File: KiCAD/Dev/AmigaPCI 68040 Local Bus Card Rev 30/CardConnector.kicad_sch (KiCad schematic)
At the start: 29 parts, among them CN100 DIN41612_03x40, CN3 SPI, U10 ICE40HX4K-TQ144, U409F2 W25X20CLSN

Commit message: Start routing PCLB card, Rev 3.0 08-JUL-2024
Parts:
- added C135: 47uF, Capacitor_THT:CP_Radial_D5.0mm_P2.00mm, symbol AmigaPCI-Symbols:CP_Small-Device
- added C137: 0.1uF, Capacitor_SMD:C_0603_1608Metric, symbol Device:C_Small
- added J100: CPU CLOCK, Connector_PinHeader_2.54mm:PinHeader_2x02_P2.54mm_Vertical, symbol Connector_Generic:Conn_02x02_Odd_Even
- added R110, R111: 10k, Resistor_SMD:R_0603_1608Metric, symbol Device:R
- added R112, R113, R114, R115, R116, R117, R118: 22R, Resistor_SMD:R_0603_1608Metric, symbol Device:R
- added X100: 40MHz, Oscillator:Oscillator_SMD_ECS_2520MV-xxx-xx-4Pin_2.5x2.0mm, symbol Oscillator:XO32
- renumbered C16 to C122, C17 to C123, C18 to C124, C19 to C125, C20 to C126, C21 to C127, C22 to C128, C23 to C129, C24 to C130, C25 to C131, C26 to C132, C27 to C133, C28 to C134, C15 to C136, CN3 to CN111, R5 to R106, R6 to R107, R7 to R108, R8 to R109, U10 to U111
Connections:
- net +1V2: now also C135.1
- net +3V3: now also C137.1, R110.1, R111.1, X100.1 (EN), X100.4 (V+)
- net BCLKA: now also R117.2; no longer U111.20 (IO3_13B_GBIN7)
- net GND: now also C135.2, C137.2, J100.1 (Pin_1), J100.3 (Pin_3), X100.2 (GND)
- net PCLKA: now also R118.2; no longer U111.21 (IO3_14A_GBIN6)
- net _RESET: now also U111.47 (IO2_79); no longer U111.49 (IO2_81_GBIN5)
- net CLK40: now reaches U111.128 (IO0_197_GBIN1)
- net CLK40: now also R112.1
- net RAMCLK: now reaches U111.129 (IO0_198_GBIN0)
- net at U111.52 (IO2_82_GBIN4): now also R116.1
- net CLKA: now reaches U111.90 (IO1_138)
- net CLKA: now also J100.2 (Pin_2), R110.2
- net CLKB: now reaches U111.91 (IO1_139)
- net CLKB: now also J100.4 (Pin_4), R111.2
- net at U111.93 (IO1_140_GBIN3): now also R117.1
- net at U111.94 (IO1_141_GBIN2): now also R118.1
- net BCLK renamed BCLKC
- net BCLKC: now also R113.2
- net PCLK renamed PCLKC
- net PCLKC: now also R114.2
- new net: R115.1, U111.49 (IO2_81_GBIN5)
- new net: R114.1, U111.21 (IO3_14A_GBIN6)
- new net: R113.1, U111.20 (IO3_13B_GBIN7)
- new net: R112.2, X100.3 (OUT)
- new net BCLKB: R115.2
- new net PCLKB: R116.2
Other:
- note added: "BYTE SIZING"
- note added: "CLOCK STUFF"
- note added: "J100 CLOCK SPEED SELECTION -------------------------- All Open = 40/80MHz 1-2 = 33/66MHz 3-4 = 25/50MHz 1-2 & 3-4 = 16/32MHz"
- note added: "LOCAL BUS PORT"
- note added: "LOCAL BUS PORT, BYTE SIZING, CLOCKS"
- note removed: "CARD CONNECTOR"
- note removed: "CARD EDGE AND RAM"
- moved on the sheet: CN100, H1, H2

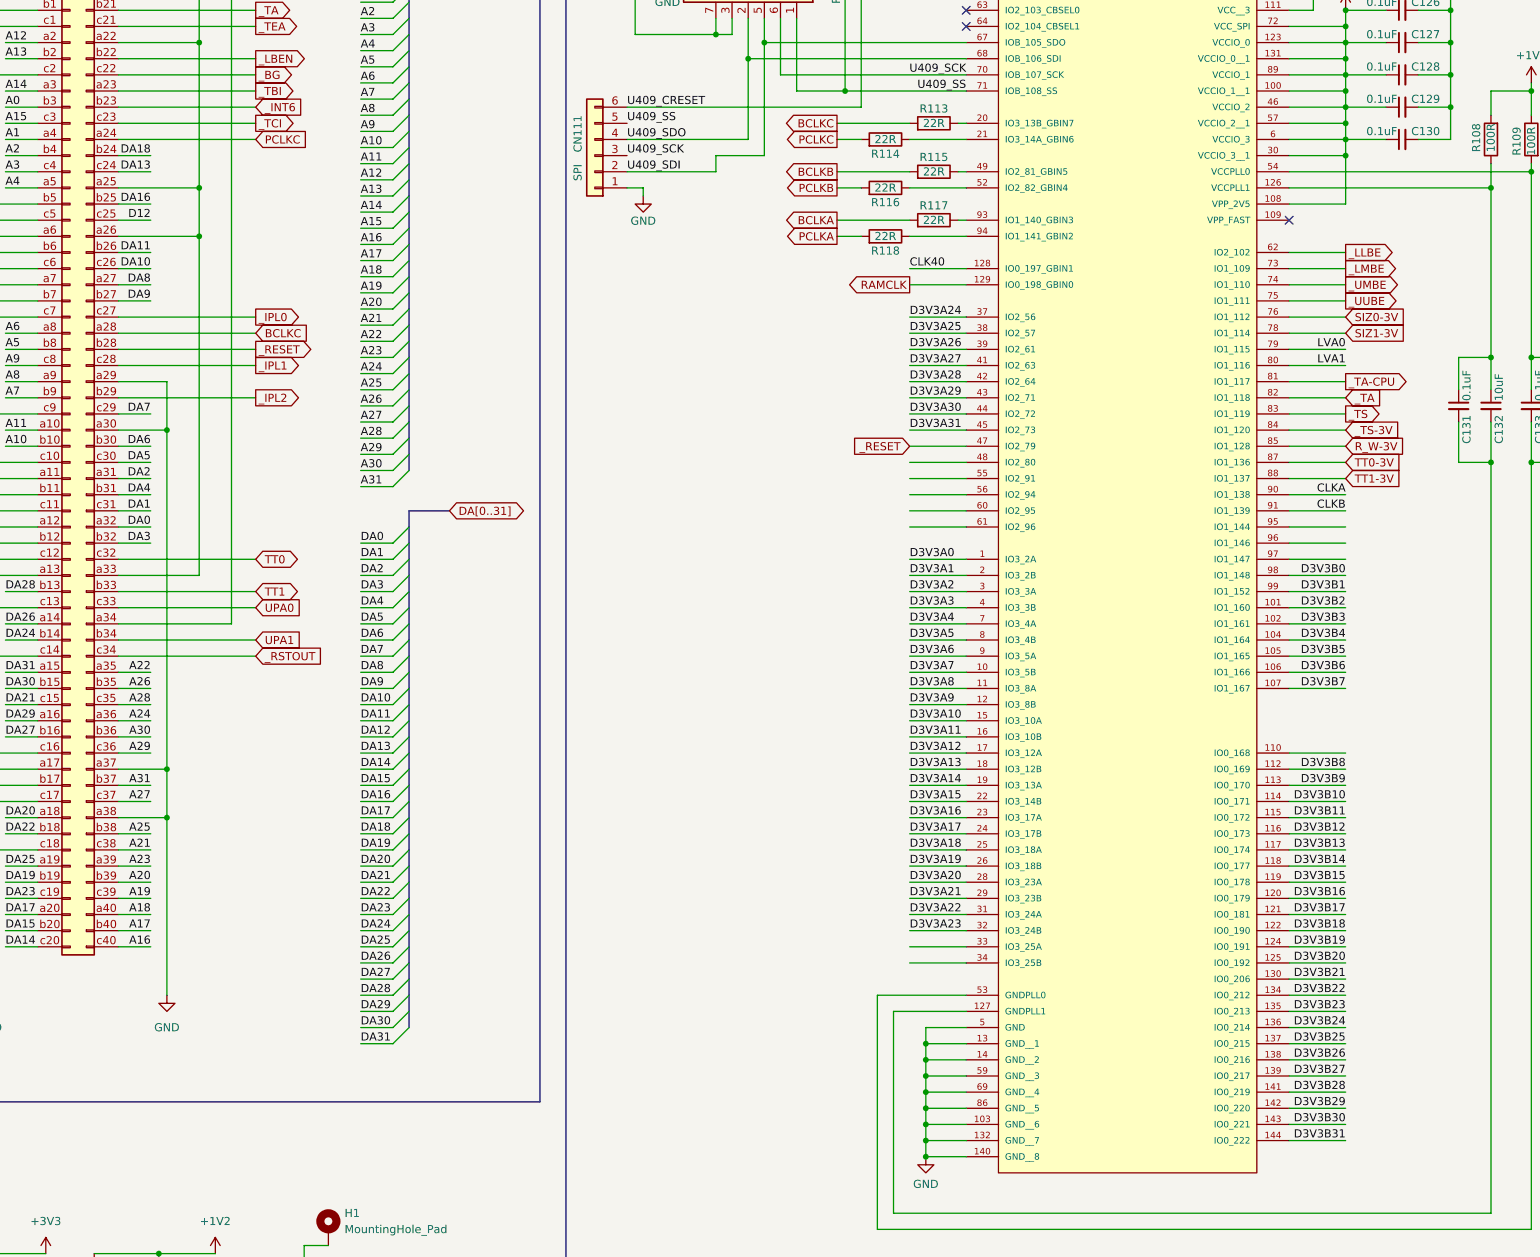
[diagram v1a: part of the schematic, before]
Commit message: PCB Routing CPU Card 10-JUL-2024
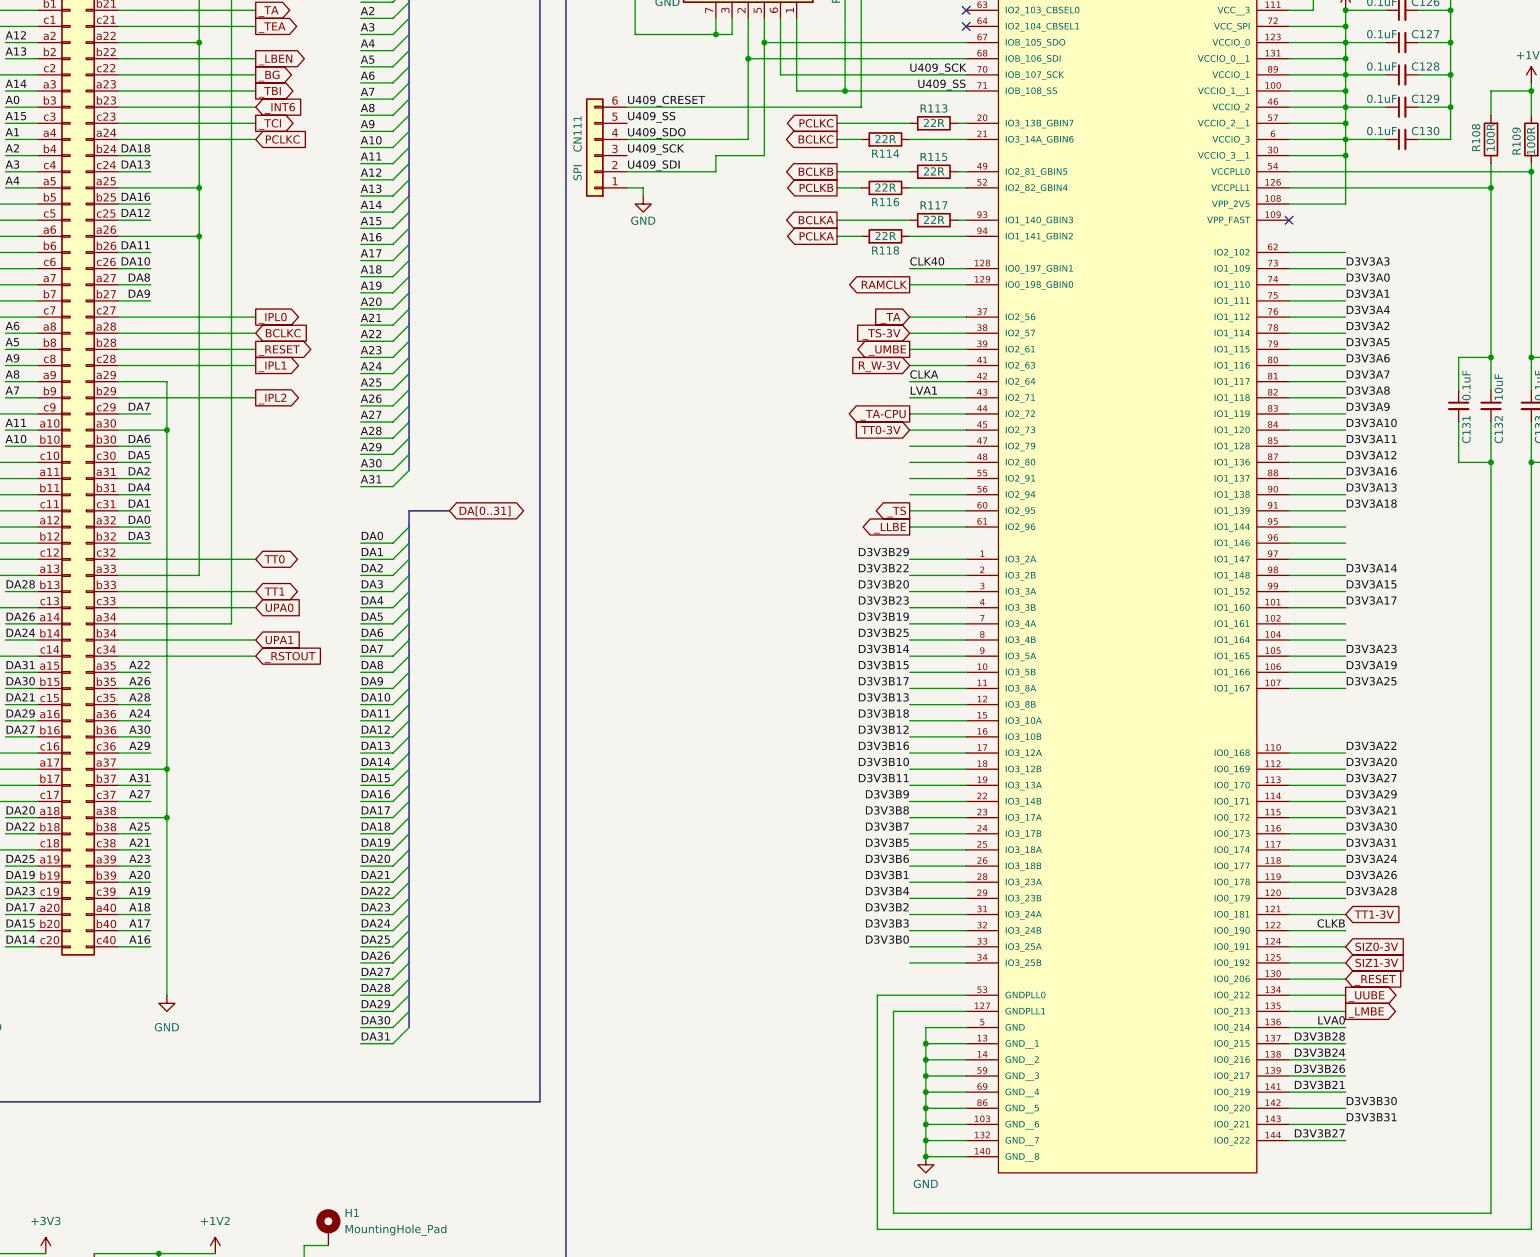
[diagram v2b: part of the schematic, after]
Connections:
- net D12 is gone; now on net DA12: CN100.c25 (Pin_c25)
- net BCLKC: now also R114.2; no longer R113.2
- net CLKA: now also U111.42 (IO2_64); no longer U111.90 (IO1_138)
- net CLKB: now also U111.122 (IO0_190); no longer U111.91 (IO1_139)
- net D3V3A0: now also U111.74 (IO1_110); no longer U111.1 (IO3_2A)
- net D3V3A1: now also U111.75 (IO1_111); no longer U111.2 (IO3_2B)
- net D3V3A10: now also U111.84 (IO1_120); no longer U111.15 (IO3_10A)
- net D3V3A11: now also U111.85 (IO1_128); no longer U111.16 (IO3_10B)
- net D3V3A12: now also U111.87 (IO1_136); no longer U111.17 (IO3_12A)
- net D3V3A13: now also U111.90 (IO1_138); no longer U111.18 (IO3_12B)
- net D3V3A14: now also U111.98 (IO1_148); no longer U111.19 (IO3_13A)
- net D3V3A15: now also U111.99 (IO1_152); no longer U111.22 (IO3_14B)
- net D3V3A16: now also U111.88 (IO1_137); no longer U111.23 (IO3_17A)
- net D3V3A17: now also U111.101 (IO1_160); no longer U111.24 (IO3_17B)
- net D3V3A18: now also U111.91 (IO1_139); no longer U111.25 (IO3_18A)
- net D3V3A19: now also U111.106 (IO1_166); no longer U111.26 (IO3_18B)
- net D3V3A2: now also U111.78 (IO1_114); no longer U111.3 (IO3_3A)
- net D3V3A20: now also U111.112 (IO0_169); no longer U111.28 (IO3_23A)
- net D3V3A21: now also U111.115 (IO0_172); no longer U111.29 (IO3_23B)
- net D3V3A22: now also U111.110 (IO0_168); no longer U111.31 (IO3_24A)
- net D3V3A23: now also U111.105 (IO1_165); no longer U111.32 (IO3_24B)
- net D3V3A24: now also U111.118 (IO0_177); no longer U111.37 (IO2_56)
- net D3V3A25: now also U111.107 (IO1_167); no longer U111.38 (IO2_57)
- net D3V3A26: now also U111.119 (IO0_178); no longer U111.39 (IO2_61)
- net D3V3A27: now also U111.113 (IO0_170); no longer U111.41 (IO2_63)
- net D3V3A28: now also U111.120 (IO0_179); no longer U111.42 (IO2_64)
- net D3V3A29: now also U111.114 (IO0_171); no longer U111.43 (IO2_71)
- net D3V3A3: now also U111.73 (IO1_109); no longer U111.4 (IO3_3B)
- net D3V3A30: now also U111.116 (IO0_173); no longer U111.44 (IO2_72)
- net D3V3A31: now also U111.117 (IO0_174); no longer U111.45 (IO2_73)
- net D3V3A4: now also U111.76 (IO1_112); no longer U111.7 (IO3_4A)
- net D3V3A5: now also U111.79 (IO1_115); no longer U111.8 (IO3_4B)
- net D3V3A6: now also U111.80 (IO1_116); no longer U111.9 (IO3_5A)
- net D3V3A7: now also U111.81 (IO1_117); no longer U111.10 (IO3_5B)
- net D3V3A8: now also U111.82 (IO1_118); no longer U111.11 (IO3_8A)
- net D3V3A9: now also U111.83 (IO1_119); no longer U111.12 (IO3_8B)
- net D3V3B0: now also U111.33 (IO3_25A); no longer U111.98 (IO1_148)
- net D3V3B1: now also U111.28 (IO3_23A); no longer U111.99 (IO1_152)
- net D3V3B10: now also U111.18 (IO3_12B); no longer U111.114 (IO0_171)
- net D3V3B11: now also U111.19 (IO3_13A); no longer U111.115 (IO0_172)
- net D3V3B12: now also U111.16 (IO3_10B); no longer U111.116 (IO0_173)
- net D3V3B13: now also U111.12 (IO3_8B); no longer U111.117 (IO0_174)
- net D3V3B14: now also U111.9 (IO3_5A); no longer U111.118 (IO0_177)
- net D3V3B15: now also U111.10 (IO3_5B); no longer U111.119 (IO0_178)
- net D3V3B16: now also U111.17 (IO3_12A); no longer U111.120 (IO0_179)
- net D3V3B17: now also U111.11 (IO3_8A); no longer U111.121 (IO0_181)
- net D3V3B18: now also U111.15 (IO3_10A); no longer U111.122 (IO0_190)
- net D3V3B19: now also U111.7 (IO3_4A); no longer U111.124 (IO0_191)
- net D3V3B2: now also U111.31 (IO3_24A); no longer U111.101 (IO1_160)
- net D3V3B20: now also U111.3 (IO3_3A); no longer U111.125 (IO0_192)
- net D3V3B21: now also U111.141 (IO0_219); no longer U111.130 (IO0_206)
- net D3V3B22: now also U111.2 (IO3_2B); no longer U111.134 (IO0_212)
- net D3V3B23: now also U111.4 (IO3_3B); no longer U111.135 (IO0_213)
- net D3V3B24: now also U111.138 (IO0_216); no longer U111.136 (IO0_214)
- net D3V3B25: now also U111.8 (IO3_4B); no longer U111.137 (IO0_215)
- net D3V3B26: now also U111.139 (IO0_217); no longer U111.138 (IO0_216)
- net D3V3B27: now also U111.144 (IO0_222); no longer U111.139 (IO0_217)
- net D3V3B28: now also U111.137 (IO0_215); no longer U111.141 (IO0_219)
- net D3V3B29: now also U111.1 (IO3_2A); no longer U111.142 (IO0_220)
- net D3V3B3: now also U111.32 (IO3_24B); no longer U111.102 (IO1_161)
- net D3V3B30: now also U111.142 (IO0_220); no longer U111.143 (IO0_221)
- net D3V3B31: now also U111.143 (IO0_221); no longer U111.144 (IO0_222)
- net D3V3B4: now also U111.29 (IO3_23B); no longer U111.104 (IO1_164)
- net D3V3B5: now also U111.25 (IO3_18A); no longer U111.105 (IO1_165)
- net D3V3B6: now also U111.26 (IO3_18B); no longer U111.106 (IO1_166)
- net D3V3B7: now also U111.24 (IO3_17B); no longer U111.107 (IO1_167)
- net D3V3B8: now also U111.23 (IO3_17A); no longer U111.112 (IO0_169)
- net D3V3B9: now also U111.22 (IO3_14B); no longer U111.113 (IO0_170)
- net LVA0: now also U111.136 (IO0_214); no longer U111.79 (IO1_115)
- net LVA1: now also U111.43 (IO2_71); no longer U111.80 (IO1_116)
- net PCLKC: now also R113.2; no longer R114.2
- net R_W-3V: now also U111.41 (IO2_63); no longer U111.85 (IO1_128)
- net SIZ0-3V: now also U111.124 (IO0_191); no longer U111.76 (IO1_112)
- net SIZ1-3V: now also U111.125 (IO0_192); no longer U111.78 (IO1_114)
- net TT0-3V: now also U111.45 (IO2_73); no longer U111.87 (IO1_136)
- net TT1-3V: now also U111.121 (IO0_181); no longer U111.88 (IO1_137)
- net _LLBE: now also U111.61 (IO2_96); no longer U111.62 (IO2_102)
- net _LMBE: now also U111.135 (IO0_213); no longer U111.73 (IO1_109)
- net _RESET: now also U111.130 (IO0_206); no longer U111.47 (IO2_79)
- net _TA: now also U111.37 (IO2_56); no longer U111.82 (IO1_118)
- net _TA-CPU: now also U111.44 (IO2_72); no longer U111.81 (IO1_117)
- net _TS: now also U111.60 (IO2_95); no longer U111.83 (IO1_119)
- net _TS-3V: now also U111.38 (IO2_57); no longer U111.84 (IO1_120)
- net _UMBE: now also U111.39 (IO2_61); no longer U111.74 (IO1_110)
- net _UUBE: now also U111.134 (IO0_212); no longer U111.75 (IO1_111)

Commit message: CPU Local Bus Card Rev 3.0 Routing 15-JUL-2024
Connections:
- net GND: no longer CN100.a1 (Pin_a1)
- net LVA0: now also U111.96 (IO1_146); no longer U111.136 (IO0_214)
- net _BG: now also U111.44 (IO2_72)
- net _LBEN: now also U111.62 (IO2_102)
- net _LMBE: now also U111.95 (IO1_144); no longer U111.135 (IO0_213)
- net _TA-CPU: now also U111.55 (IO2_91); no longer U111.44 (IO2_72)
- net _TBI: now also U111.48 (IO2_80)
- net _DSACK1: now reaches U111.47 (IO2_79)
- net _DSACK1: now also CN100.b21 (Pin_b21)
- net _TS-CPU: now reaches U111.56 (IO2_94)
- net _TA renamed _DSACK0
- net _DSACK0: now also CN100.a1 (Pin_a1); no longer CN100.b21 (Pin_b21)
- new net BUFDIR: U111.136 (IO0_214)
- new net _BUFEN: U111.135 (IO0_213)
- no-connect marks 3 -> 4
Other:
- note added: "BUS SIZING"
- note added: "LOCAL BUS PORT, BUS SIZING, CLOCKS"
- note removed: "BYTE SIZING"
- note removed: "LOCAL BUS PORT, BYTE SIZING, CLOCKS"
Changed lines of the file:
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@@
 	(title_block
 		(title "AmigaPCI 68040")
-		(date "2024-07-10")
+		(date "2024-07-14")
 		(rev "3.0")
 	)
@@
 	)
 	(junction
-		(at 59.69 49.53)
-		(diameter 0)
-		(color 0 0 0 0)
-	)
-	(junction
 		(at 289.56 26.67)
 		(diameter 0)
@@
 	)
 	(no_connect
+		(at 273.05 133.35)
+	)
+	(no_connect
 		(at 213.36 49.53)
 	)
@@
 	(wire
 		(pts
+			(xy 271.78 85.09) (xy 264.16 85.09)
+		)
+		(stroke
+			(width 0)
+			(type default)
+		)
+	)
+	(wire
+		(pts
 			(xy 40.64 95.25) (xy 67.31 95.25)
 		)
@@
 		)
 	)
-	(wire
-		(pts
-			(xy 59.69 44.45) (xy 59.69 49.53)
-		)
-		(stroke
-			(width 0)
-			(type default)
-		)
-	)
 	(bus
 		(pts
@@
 	(wire
 		(pts
+			(xy 271.78 82.55) (xy 271.78 85.09)
+		)
+		(stroke
+			(width 0)
+			(type default)
+		)
+	)
+	(wire
+		(pts
 			(xy 118.11 55.88) (xy 123.19 55.88)
 		)
@@
 	(wire
 		(pts
-			(xy 67.31 44.45) (xy 59.69 44.45)
+			(xy 67.31 44.45) (xy 38.1 44.45)
 		)
 		(stroke
@@
 	(wire
 		(pts
-			(xy 264.16 85.09) (xy 273.05 85.09)
+			(xy 271.78 82.55) (xy 273.05 82.55)
 		)
 		(stroke
@@
 		)
 	)
-	(text "BYTE SIZING"
+	(text "BUS SIZING"
 		(exclude_from_sim no)
 		(at 220.472 28.194 0)
@@
 		)
 	)
-	(text "LOCAL BUS PORT, \nBYTE SIZING, CLOCKS"
+	(text "LOCAL BUS PORT, \nBUS SIZING, CLOCKS"
 		(exclude_from_sim no)
 		(at 312.166 250.444 0)
@@
 	)
 	(label "LVA0"
-		(at 273.05 207.01 180)
+		(at 273.05 130.81 180)
 		(fields_autoplaced yes)
 		(effects
@@
 		)
 	)
+	(global_label "_BUFEN"
+		(shape output)
+		(at 273.05 204.47 0)
+		(effects
+			(font
+				(size 1.27 1.27)
+			)
+			(justify left)
+		)
+		(property "Intersheetrefs" "${INTERSHEET_REFS}"
+			(at 282.448 204.47 0)
+			(effects
+				(font
+					(size 1.27 1.27)
+				)
+				(justify left)
+			)
+		)
+	)
 	(global_label "_LOCKE"
 		(shape output)
@@
 		)
 	)
-	(global_label "_TA"
+	(global_label "_DSACK0"
 		(shape input)
 		(at 204.47 95.25 180)
@@
 		)
 		(property "Intersheetrefs" "${INTERSHEET_REFS}"
-			(at 198.461 95.25 0)
+			(at 193.1996 95.25 0)
 			(effects
 				(font
@@
 	(global_label "_LMBE"
 		(shape output)
-		(at 273.05 204.47 0)
+		(at 273.05 128.27 0)
 		(fields_autoplaced yes)
 		(effects
@@
 		)
 		(property "Intersheetrefs" "${INTERSHEET_REFS}"
-			(at 281.9013 204.47 0)
+			(at 281.9013 128.27 0)
 			(effects
 				(font
@@
 		)
 	)
+	(global_label "BUFDIR"
+		(shape output)
+		(at 273.05 207.01 0)
+		(effects
+			(font
+				(size 1.27 1.27)
+			)
+			(justify left)
+		)
+		(property "Intersheetrefs" "${INTERSHEET_REFS}"
+			(at 281.94 207.01 0)
+			(effects
+				(font
+					(size 1.27 1.27)
+				)
+				(justify left)
+			)
+		)
+	)
 	(global_label "_TS"
 		(shape bidirectional)
@@
 		)
 	)
+	(global_label "_DSACK0"
+		(shape output)
+		(at 38.1 44.45 180)
+		(fields_autoplaced yes)
+		(effects
+			(font
+				(size 1.27 1.27)
+			)
+			(justify right)
+		)
+		(property "Intersheetrefs" "${INTERSHEET_REFS}"
+			(at 26.8296 44.45 0)
+			(effects
+				(font
+					(size 1.27 1.27)
+				)
+				(justify right)
+			)
+		)
+	)
 	(global_label "TM0"
 		(shape output)
@@
 		)
 	)
+	(global_label "_TBI"
+		(shape input)
+		(at 204.47 118.11 180)
+		(fields_autoplaced yes)
+		(effects
+			(font
+				(size 1.27 1.27)
+			)
+			(justify right)
+		)
+		(property "Intersheetrefs" "${INTERSHEET_REFS}"
+			(at 197.6748 118.11 0)
+			(effects
+				(font
+					(size 1.27 1.27)
+				)
+				(justify right)
+			)
+		)
+	)
+	(global_label "_DSACK1"
+		(shape input)
+		(at 204.47 115.57 180)
+		(fields_autoplaced yes)
+		(effects
+			(font
+				(size 1.27 1.27)
+			)
+			(justify right)
+		)
+		(property "Intersheetrefs" "${INTERSHEET_REFS}"
+			(at 193.1996 115.57 0)
+			(effects
+				(font
+					(size 1.27 1.27)
+				)
+				(justify right)
+			)
+		)
+	)
+	(global_label "_LBEN"
+		(shape input)
+		(at 273.05 82.55 0)
+		(fields_autoplaced yes)
+		(effects
+			(font
+				(size 1.27 1.27)
+			)
+			(justify left)
+		)
+		(property "Intersheetrefs" "${INTERSHEET_REFS}"
+			(at 281.7804 82.55 0)
+			(effects
+				(font
+					(size 1.27 1.27)
+				)
+				(justify left)
+			)
+		)
+	)
+	(global_label "_TS-CPU"
+		(shape input)
+		(at 204.47 123.19 180)
+		(fields_autoplaced yes)
+		(effects
+			(font
+				(size 1.27 1.27)
+			)
+			(justify right)
+		)
+		(property "Intersheetrefs" "${INTERSHEET_REFS}"
+			(at 192.8972 123.19 0)
+			(effects
+				(font
+					(size 1.27 1.27)
+				)
+				(justify right)
+			)
+		)
+	)
 	(global_label "_TCI"
 		(shape output)
@@
 		)
 	)
-	(global_label "_TA-CPU"
-		(shape output)
+	(global_label "_BG"
+		(shape input)
 		(at 204.47 110.49 180)
 		(fields_autoplaced yes)
@@
 		)
 		(property "Intersheetrefs" "${INTERSHEET_REFS}"
-			(at 193.0181 110.49 0)
+			(at 197.9772 110.49 0)
 			(effects
 				(font
@@
 		)
 	)
-	(global_label "_TA"
+	(global_label "_DSACK1"
 		(shape output)
 		(at 101.6 46.99 0)
@@
 		)
 		(property "Intersheetrefs" "${INTERSHEET_REFS}"
-			(at 107.609 46.99 0)
+			(at 112.8704 46.99 0)
 			(effects
 				(font
@@
 	)
 	(global_label "_LBEN"
-		(shape output)
+		(shape input)
 		(at 101.6 54.61 0)
 		(fields_autoplaced yes)
@@
 			(effects
 				(font
+					(size 1.27 1.27)
+				)
+				(justify right)
+			)
+		)
+	)
+	(global_label "_TA-CPU"
+		(shape output)
+		(at 204.47 120.65 180)
+		(fields_autoplaced yes)
+		(effects
+			(font
+				(size 1.27 1.27)
+			)
+			(justify right)
+		)
+		(property "Intersheetrefs" "${INTERSHEET_REFS}"
+			(at 193.0181 120.65 0)
+			(effects
+				(font
